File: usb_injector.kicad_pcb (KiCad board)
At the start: 2 copper layers, 38.1 x 22.1 mm, 10 parts, among them J1 USB_MALE, J2 USB_FEMALE, J3 USB_FEMALE_WITH_ID, J4 USB_FEMALE_WITH_ID, J5 USB_MALE, J6 USB_FEMALE, J7 USB_FEMALE_WITH_ID, J8 USB_FEMALE_WITH_ID, P1 CONN_6, P2 CONN_6

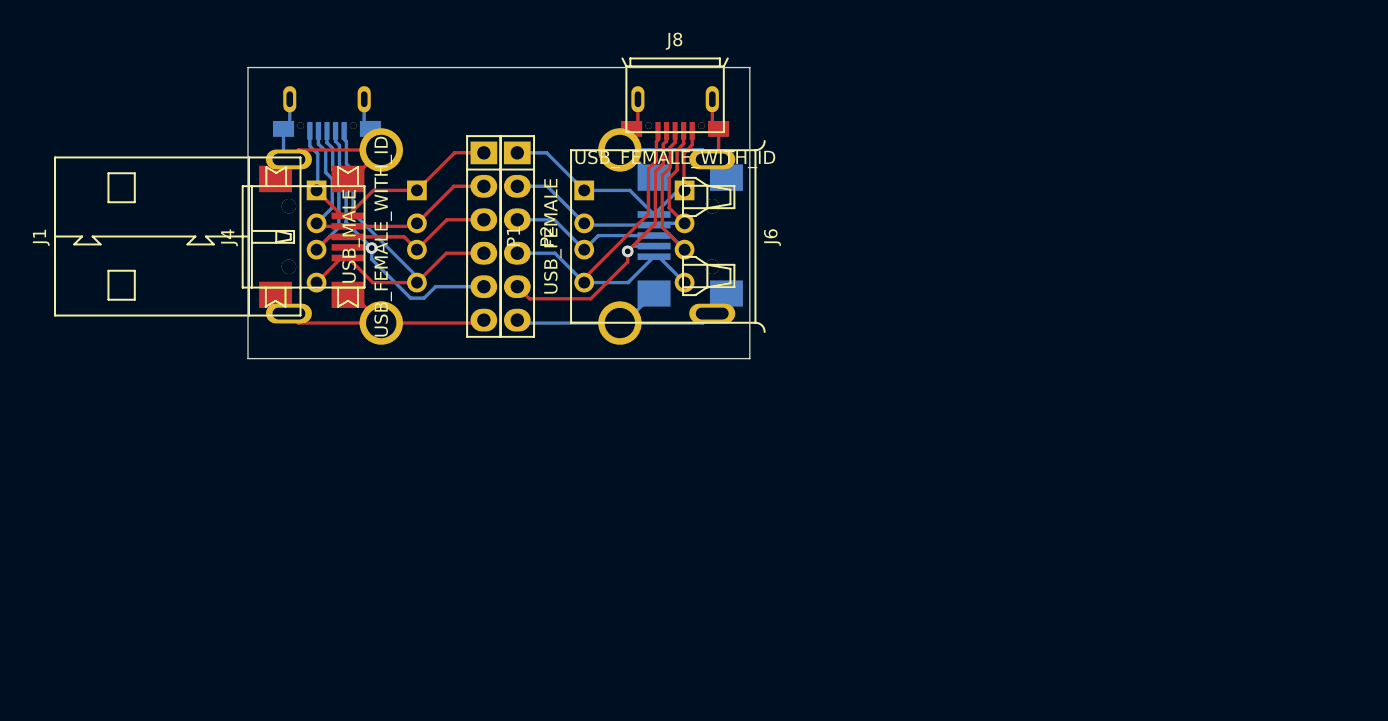
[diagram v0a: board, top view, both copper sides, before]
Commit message: changed footprints to comply with KiCad Library Conventions and moved board/components so that the board aligns with a 5mm grid
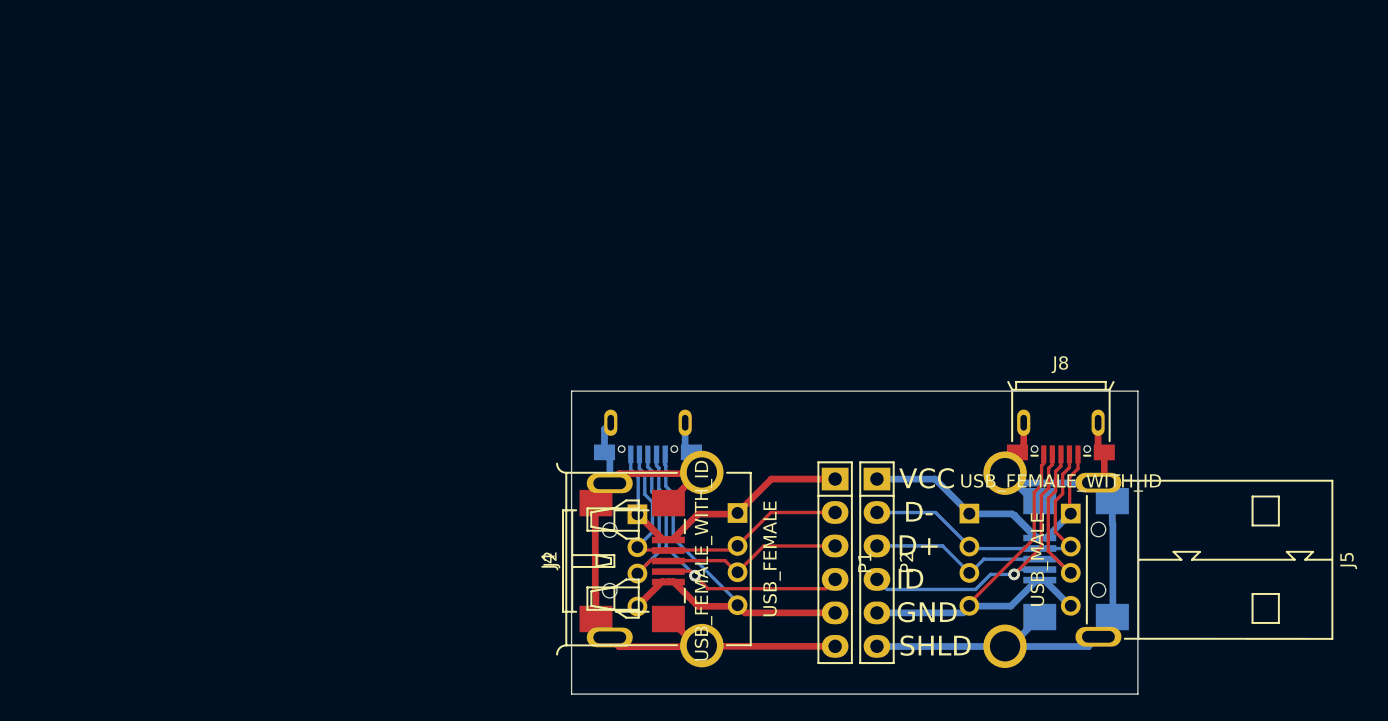
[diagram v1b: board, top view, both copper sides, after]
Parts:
- J1, J6: moved to B.Cu
- J2, J5: moved to F.Cu
- moved J8 39.3 mm to (98.5, 64.8), turned to 180 degrees
- moved J7 37.2 mm to (95.5, 71.2), turned to 270 degrees
- moved P2 36.9 mm to (83.2, 73.0)
- moved P1 36.4 mm to (80.0, 73.0)
- moved J5 36.1 mm to (97.9, 69.3), turned to 270 degrees
- moved J6 36.0 mm to (90.2, 69.3)
- moved J3 33.8 mm to (64.5, 64.8), turned to 0 degrees
- moved J4 33.5 mm to (67.3, 71.3), turned to 270 degrees
- moved J1 32.2 mm to (65.0, 69.3), turned to 270 degrees
- moved J2 32.1 mm to (72.6, 69.2)
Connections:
- P1 pad 4: Net-(J1-Pad4) -> Net-(J3-Pad4)
- P1 pad 5: Net-(J3-Pad4) -> Net-(J1-Pad4)
- P2 pad 4: Net-(J5-Pad4) -> Net-(J7-Pad4)
- P2 pad 5: Net-(J7-Pad4) -> Net-(J5-Pad4)
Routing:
- net Net-(J1-Pad5): track 42.7 -> 55.1 mm
- net Net-(J5-Pad5): track 42.7 -> 53.4 mm
- net Net-(J5-Pad1): track 20.2 -> 28.2 mm
- net Net-(J1-Pad1): track 20.3 -> 22.5 mm
- net Net-(J1-Pad3): track 24.5 -> 26.7 mm
- net Net-(J1-Pad2): track 22.0 -> 24.2 mm
- net Net-(J5-Pad3): track 24.7 -> 26.5 mm
- net Net-(J5-Pad2): track 21.9 -> 23.8 mm
- net Net-(J3-Pad4): track 22.8 -> 24.6 mm
- net Net-(J1-Pad4): track 29.0 -> 30.6 mm
- net Net-(J5-Pad4): track 29.1 -> 30.4 mm
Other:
- board size 38.1 x 22.1 mm -> 43 x 23 mm
- board text added: "D+"
- board text added: "D-"
- board text added: "GND"
- board text added: "ID"
- board text added: "SHLD"
- board text added: "USB INJECTOR V1.0"
- board text added: "VCC"
